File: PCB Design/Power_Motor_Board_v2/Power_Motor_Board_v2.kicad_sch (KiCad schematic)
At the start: 38 parts, among them IC1 DRV8251ADDAR, IC3 DRV8251ADDAR, IC4 AP63205WU-7, J1 691137710002, J2 691137710002, J2A1 SSW-119-01-T-D, J3 691137710002, J4 Conn_01x06, J5 Conn_01x02_Socket

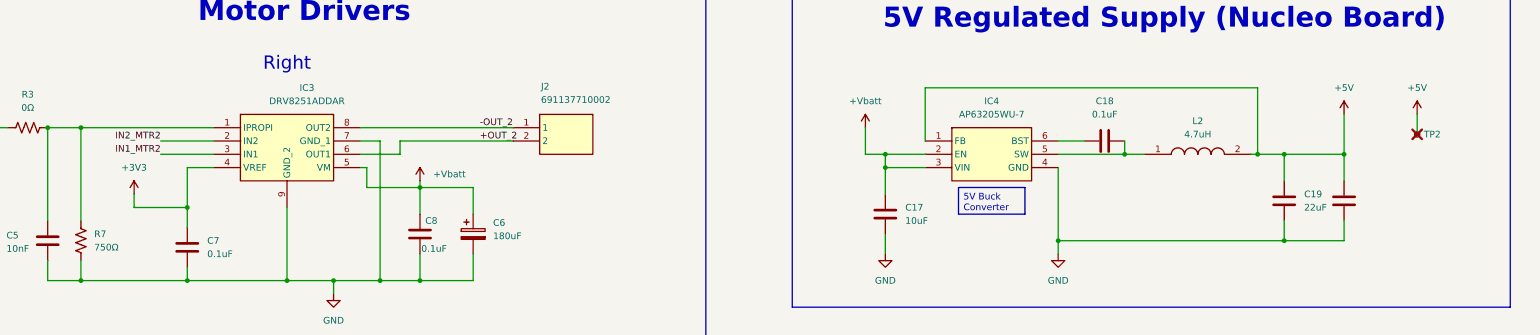
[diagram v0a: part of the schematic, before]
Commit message: Continued board layout and mesurements as well as edited BOM
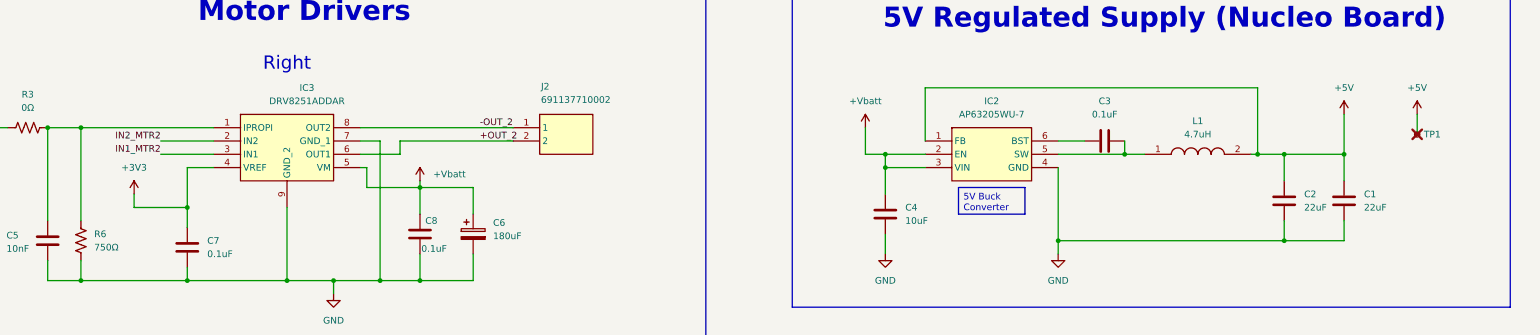
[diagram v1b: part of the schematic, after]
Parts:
- R1, R3, R4, R5: footprint Resistor_SMD:R_1206_3216Metric_Pad1.30x1.75mm_HandSolder -> Resistor_SMD:R_0805_2012Metric_Pad1.20x1.40mm_HandSolder
- renumbered C20 to C1, C19 to C2, C18 to C3, C17 to C4, IC4 to IC2, L2 to L1, R7 to R6, TP2 to TP1
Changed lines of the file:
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@@
 		)
 	)
-	(label ""
-		(at 55.88 241.3 0)
-		(effects
-			(font
-				(size 1.27 1.27)
-			)
-			(justify left bottom)
-		)
-	)
 	(label "EN"
 		(at 121.92 199.39 180)
@@
 		(dnp no)
 		(fields_autoplaced yes)
-		(property "Reference" "L2"
+		(property "Reference" "L1"
 			(at 318.77 48.26 0)
 			(effects
@@
 			(project "Power_Motor_Board_v2"
 				(path "/40d448a0-a1e3-45a7-b449-e8a8a995c831"
-					(reference "L2")
+					(reference "L1")
 					(unit 1)
 				)
@@
 		(dnp no)
 		(fields_autoplaced yes)
-		(property "Reference" "C17"
+		(property "Reference" "C4"
 			(at 262.89 64.7699 0)
 			(effects
@@
 			(project "Power_Motor_Board_v2"
 				(path "/40d448a0-a1e3-45a7-b449-e8a8a995c831"
-					(reference "C17")
+					(reference "C4")
 					(unit 1)
 				)
@@
 		(dnp no)
 		(fields_autoplaced yes)
-		(property "Reference" "C18"
+		(property "Reference" "C3"
 			(at 300.99 44.45 90)
 			(effects
@@
 			(project "Power_Motor_Board_v2"
 				(path "/40d448a0-a1e3-45a7-b449-e8a8a995c831"
-					(reference "C18")
+					(reference "C3")
 					(unit 1)
 				)
@@
 		(dnp no)
 		(fields_autoplaced yes)
-		(property "Reference" "C20"
+		(property "Reference" "C1"
 			(at 350.52 62.2299 0)
 			(effects
@@
 				)
 				(justify right)
-				(hide yes)
 			)
 		)
@@
 				)
 				(justify right)
-				(hide yes)
 			)
 		)
@@
 			(project "Power_Motor_Board_v2"
 				(path "/40d448a0-a1e3-45a7-b449-e8a8a995c831"
-					(reference "C20")
+					(reference "C1")
 					(unit 1)
 				)
@@
 			)
 		)
-		(property "Footprint" "Resistor_SMD:R_1206_3216Metric_Pad1.30x1.75mm_HandSolder"
+		(property "Footprint" "Resistor_SMD:R_0805_2012Metric_Pad1.20x1.40mm_HandSolder"
 			(at 113.284 188.214 90)
 			(effects
@@
 		(dnp no)
 		(fields_autoplaced yes)
-		(property "Reference" "C19"
+		(property "Reference" "C2"
 			(at 339.09 62.2299 0)
 			(effects
@@
 			(project "Power_Motor_Board_v2"
 				(path "/40d448a0-a1e3-45a7-b449-e8a8a995c831"
-					(reference "C19")
+					(reference "C2")
 					(unit 1)
 				)
@@
 			)
 		)
-		(property "Footprint" "Resistor_SMD:R_1206_3216Metric_Pad1.30x1.75mm_HandSolder"
+		(property "Footprint" "Resistor_SMD:R_0805_2012Metric_Pad1.20x1.40mm_HandSolder"
 			(at 95.504 48.514 90)
 			(effects
@@
 			)
 		)
-		(property "Footprint" "Resistor_SMD:R_1206_3216Metric_Pad1.30x1.75mm_HandSolder"
+		(property "Footprint" "Resistor_SMD:R_0805_2012Metric_Pad1.20x1.40mm_HandSolder"
 			(at 113.284 190.754 90)
 			(effects
@@
 		(dnp yes)
 		(fields_autoplaced yes)
-		(property "Reference" "TP2"
+		(property "Reference" "TP1"
 			(at 361.95 50.7999 0)
 			(effects
@@
 			(project "Power_Motor_Board_v2"
 				(path "/40d448a0-a1e3-45a7-b449-e8a8a995c831"
-					(reference "TP2")
+					(reference "TP1")
 					(unit 1)
 				)
@@
 			)
 		)
-		(property "Footprint" "Resistor_SMD:R_1206_3216Metric_Pad1.30x1.75mm_HandSolder"
+		(property "Footprint" "Resistor_SMD:R_0805_2012Metric_Pad1.20x1.40mm_HandSolder"
 			(at 89.154 115.824 90)
 			(effects
@@
 		(dnp no)
 		(fields_autoplaced yes)
-		(property "Reference" "R7"
+		(property "Reference" "R6"
 			(at 107.95 69.8499 0)
 			(effects
@@
 			(project "Power_Motor_Board_v2"
 				(path "/40d448a0-a1e3-45a7-b449-e8a8a995c831"
-					(reference "R7")
+					(reference "R6")
 					(unit 1)
 				)
@@
 		(dnp no)
 		(fields_autoplaced yes)
-		(property "Reference" "IC4"
+		(property "Reference" "IC2"
 			(at 279.4 44.45 0)
 			(effects
@@
 			(project "Power_Motor_Board_v2"
 				(path "/40d448a0-a1e3-45a7-b449-e8a8a995c831"
-					(reference "IC4")
+					(reference "IC2")
 					(unit 1)
 				)

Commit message: traced out the layout
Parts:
- R1, R3, R4, R5: footprint Resistor_SMD:R_0805_2012Metric_Pad1.20x1.40mm_HandSolder -> Resistor_SMD:R_1206_3216Metric_Pad1.30x1.75mm_HandSolder
- renumbered C4 to C17, C3 to C18, C2 to C19, C1 to C20, IC2 to IC4, L1 to L2, R6 to R7, TP1 to TP2
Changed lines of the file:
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@@
 		(dnp no)
 		(fields_autoplaced yes)
-		(property "Reference" "L1"
+		(property "Reference" "L2"
 			(at 318.77 48.26 0)
 			(effects
@@
 			(project "Power_Motor_Board_v2"
 				(path "/40d448a0-a1e3-45a7-b449-e8a8a995c831"
-					(reference "L1")
+					(reference "L2")
 					(unit 1)
 				)
@@
 		(dnp no)
 		(fields_autoplaced yes)
-		(property "Reference" "C4"
+		(property "Reference" "C17"
 			(at 262.89 64.7699 0)
 			(effects
@@
 			(project "Power_Motor_Board_v2"
 				(path "/40d448a0-a1e3-45a7-b449-e8a8a995c831"
-					(reference "C4")
+					(reference "C17")
 					(unit 1)
 				)
@@
 		(dnp no)
 		(fields_autoplaced yes)
-		(property "Reference" "C3"
+		(property "Reference" "C18"
 			(at 300.99 44.45 90)
 			(effects
@@
 			(project "Power_Motor_Board_v2"
 				(path "/40d448a0-a1e3-45a7-b449-e8a8a995c831"
-					(reference "C3")
+					(reference "C18")
 					(unit 1)
 				)
@@
 		(dnp no)
 		(fields_autoplaced yes)
-		(property "Reference" "C1"
+		(property "Reference" "C20"
 			(at 350.52 62.2299 0)
 			(effects
@@
 				)
 				(justify right)
+				(hide yes)
 			)
 		)
@@
 				)
 				(justify right)
+				(hide yes)
 			)
 		)
@@
 			(project "Power_Motor_Board_v2"
 				(path "/40d448a0-a1e3-45a7-b449-e8a8a995c831"
-					(reference "C1")
+					(reference "C20")
 					(unit 1)
 				)
@@
 			)
 		)
-		(property "Footprint" "Resistor_SMD:R_0805_2012Metric_Pad1.20x1.40mm_HandSolder"
+		(property "Footprint" "Resistor_SMD:R_1206_3216Metric_Pad1.30x1.75mm_HandSolder"
 			(at 113.284 188.214 90)
 			(effects
@@
 		(dnp no)
 		(fields_autoplaced yes)
-		(property "Reference" "C2"
+		(property "Reference" "C19"
 			(at 339.09 62.2299 0)
 			(effects
@@
 			(project "Power_Motor_Board_v2"
 				(path "/40d448a0-a1e3-45a7-b449-e8a8a995c831"
-					(reference "C2")
+					(reference "C19")
 					(unit 1)
 				)
@@
 			)
 		)
-		(property "Footprint" "Resistor_SMD:R_0805_2012Metric_Pad1.20x1.40mm_HandSolder"
+		(property "Footprint" "Resistor_SMD:R_1206_3216Metric_Pad1.30x1.75mm_HandSolder"
 			(at 95.504 48.514 90)
 			(effects
@@
 			)
 		)
-		(property "Footprint" "Resistor_SMD:R_0805_2012Metric_Pad1.20x1.40mm_HandSolder"
+		(property "Footprint" "Resistor_SMD:R_1206_3216Metric_Pad1.30x1.75mm_HandSolder"
 			(at 113.284 190.754 90)
 			(effects
@@
 		(dnp yes)
 		(fields_autoplaced yes)
-		(property "Reference" "TP1"
+		(property "Reference" "TP2"
 			(at 361.95 50.7999 0)
 			(effects
@@
 			(project "Power_Motor_Board_v2"
 				(path "/40d448a0-a1e3-45a7-b449-e8a8a995c831"
-					(reference "TP1")
+					(reference "TP2")
 					(unit 1)
 				)
@@
 			)
 		)
-		(property "Footprint" "Resistor_SMD:R_0805_2012Metric_Pad1.20x1.40mm_HandSolder"
+		(property "Footprint" "Resistor_SMD:R_1206_3216Metric_Pad1.30x1.75mm_HandSolder"
 			(at 89.154 115.824 90)
 			(effects
@@
 		(dnp no)
 		(fields_autoplaced yes)
-		(property "Reference" "R6"
+		(property "Reference" "R7"
 			(at 107.95 69.8499 0)
 			(effects
@@
 			(project "Power_Motor_Board_v2"
 				(path "/40d448a0-a1e3-45a7-b449-e8a8a995c831"
-					(reference "R6")
+					(reference "R7")
 					(unit 1)
 				)
@@
 		(dnp no)
 		(fields_autoplaced yes)
-		(property "Reference" "IC2"
+		(property "Reference" "IC4"
 			(at 279.4 44.45 0)
 			(effects
@@
 			(project "Power_Motor_Board_v2"
 				(path "/40d448a0-a1e3-45a7-b449-e8a8a995c831"
-					(reference "IC2")
+					(reference "IC4")
 					(unit 1)
 				)
